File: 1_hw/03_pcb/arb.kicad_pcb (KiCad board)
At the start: 4 copper layers, 100 x 100 mm, 268 parts, among them J1 TYPE-C-31-M-12, J2 SMA, J3 SMA, J4 BNC, J5 PH-00244, SW1 TS-1187A-B-A-B, SW2 SS-12D02-VG4, SW3 SS-12D02-VG4, U1 TLV70333DBV, U10 LMK1C1103PWR, U11 STM32F446ZETx, U12 ICE40UP5K-SG48ITR, U13 93LC56BT-I_OT, U14 FT2232HL, U15 W25Q128JVSIQ, U16 W25Q128JVSIQ, U17 AD9850, U18 AD9744, U19 LM6171, U2 TLV76133DCY, U20 LM6171, U21 TMUX6104, U22 TPL0401B-10, U23 THS3491, U24 ADG1219BRJZ, U25 LM6171, U26 TMUX6104, U3 TLV70333DBV, U4 LM3880MF-1AA, U5 TLV70312DBV, U6 TLV70325DBV, U7 TPS65131RGE, U8 TPD2E001DRL, U9 ADG1219BRJZ, X1 ASE-10.000MHz, X2 ASE-100.000MHz, Y1 32.768k, Y2 12 MHz

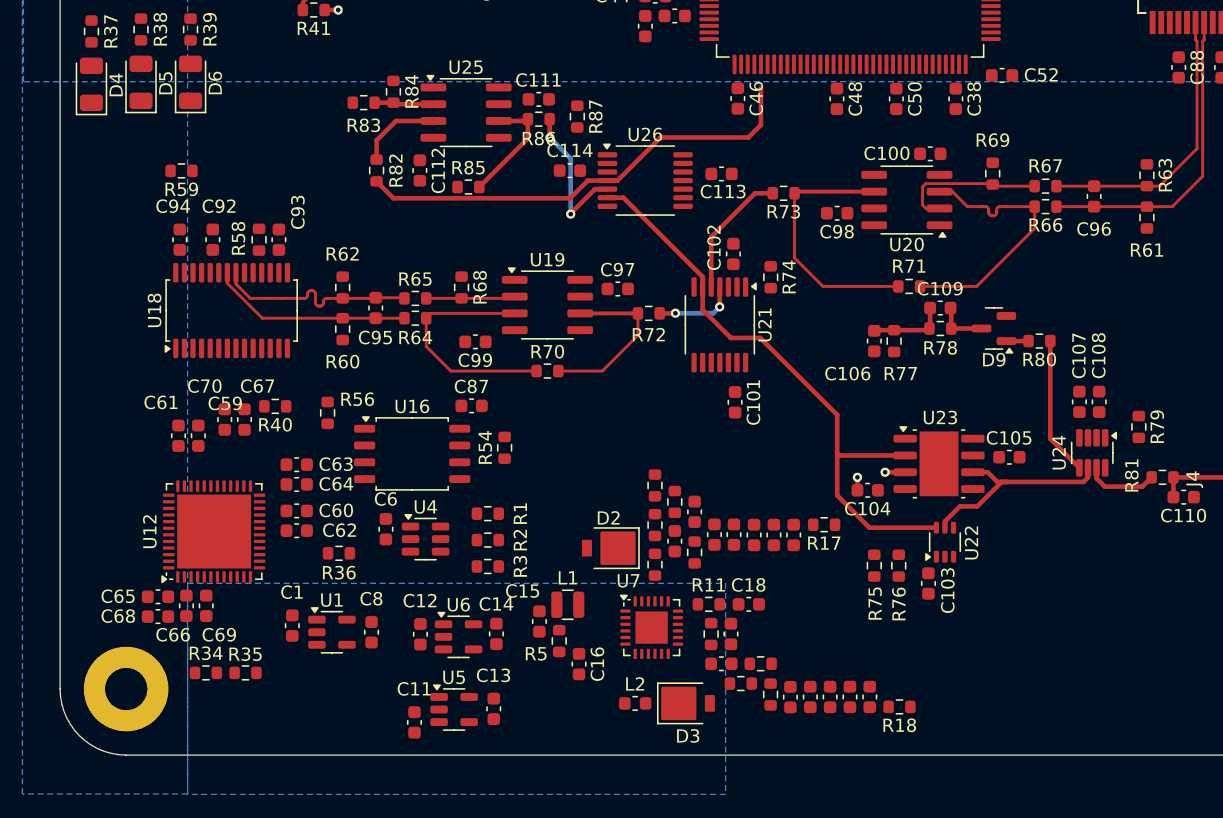
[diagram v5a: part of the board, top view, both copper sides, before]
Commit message: MINOR: Continuing layout. Laid Out FPGA Power.
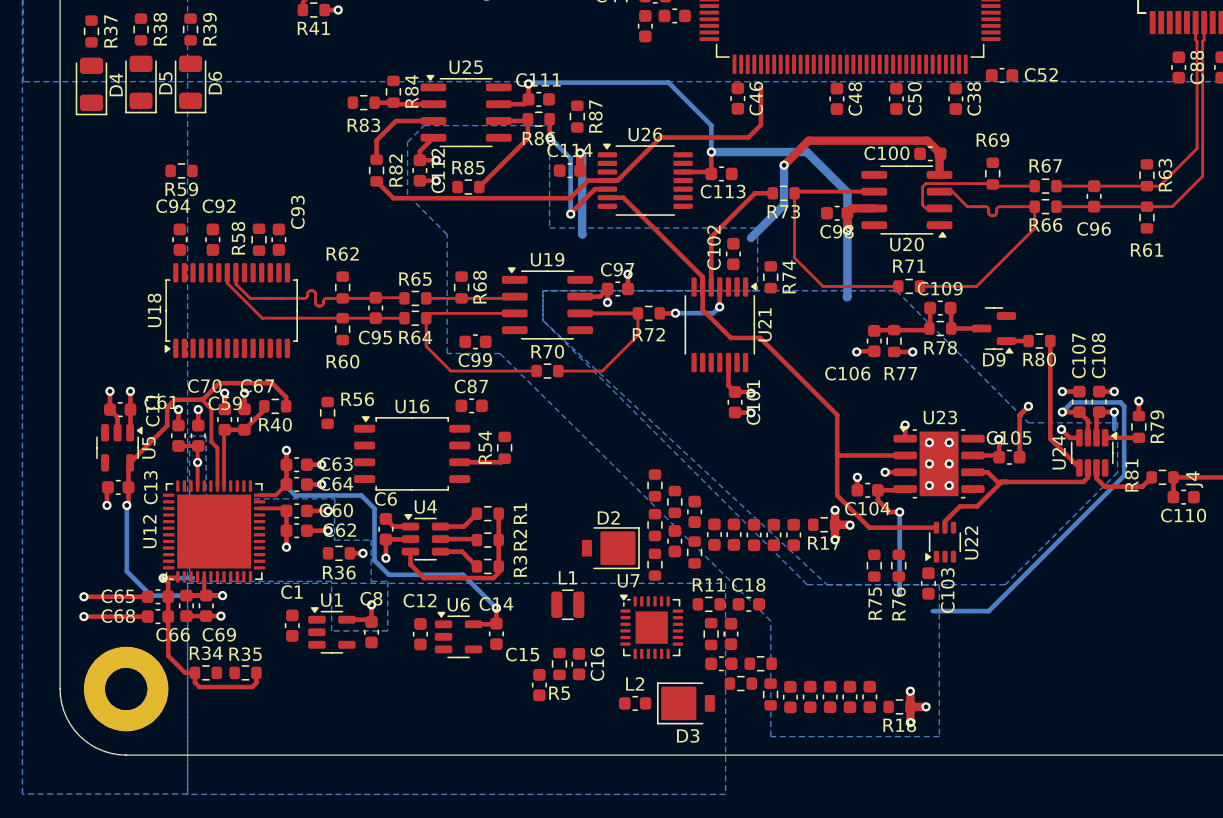
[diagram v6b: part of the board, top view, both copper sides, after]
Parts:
- moved C13 33.0 mm to (105.1, 122.7), turned to 180 degrees
- moved C11 32.5 mm to (105.2, 116.8), turned to 180 degrees
- moved U5 32.3 mm to (105.0, 119.7), turned to -90 degrees
- moved C15 4.81 mm to (137.0, 137.7)
- moved R5 1.74 mm to (138.5, 136.1), turned to 90 degrees
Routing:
- net N15P0V_A: track 0.00 -> 79.4 mm, vias 0 -> 8
- net 15P0V_A: track 0.00 -> 66.0 mm, vias 0 -> 10
- net GND: track 64.7 -> 113.0 mm, vias 41 -> 72
- net 1P2V_D: track 0.00 -> 43.9 mm, vias 0 -> 2
- net 2P5V_D: track 0.00 -> 32.6 mm, vias 0 -> 2
- net 3P3V_D_FPGA: track 0.00 -> 32.1 mm, vias 0 -> 5
- net 3P3V_D: track 37.2 -> 50.0 mm
- net Net-(U12D-VCCPLL): track 0.00 -> 8.18 mm
- net 5P0V: track 16.4 -> 21.7 mm, vias 8 -> 9
- net SPI_SCLK_MCU_FPGA_3P3: track 0.00 -> 3.51 mm
- net GPIO_2P5-EN_SEQ_REG_3P3: track 0.00 -> 3.22 mm
- net GPIO_1P2-EN_SEQ_REG_3P3: track 0.00 -> 3.15 mm
- net GPIO_3P3-EN_SEQ_REG_3P3: track 0.00 -> 2.78 mm
- net GPIO_EN_MCU_AMUX2_3P3: track 0.00 -> 2.55 mm
- added copper zone on B.Cu, net 15P0V_A
- added copper zone on B.Cu, net 3P3V_D_FPGA
- added copper zone on B.Cu, net N15P0V_A

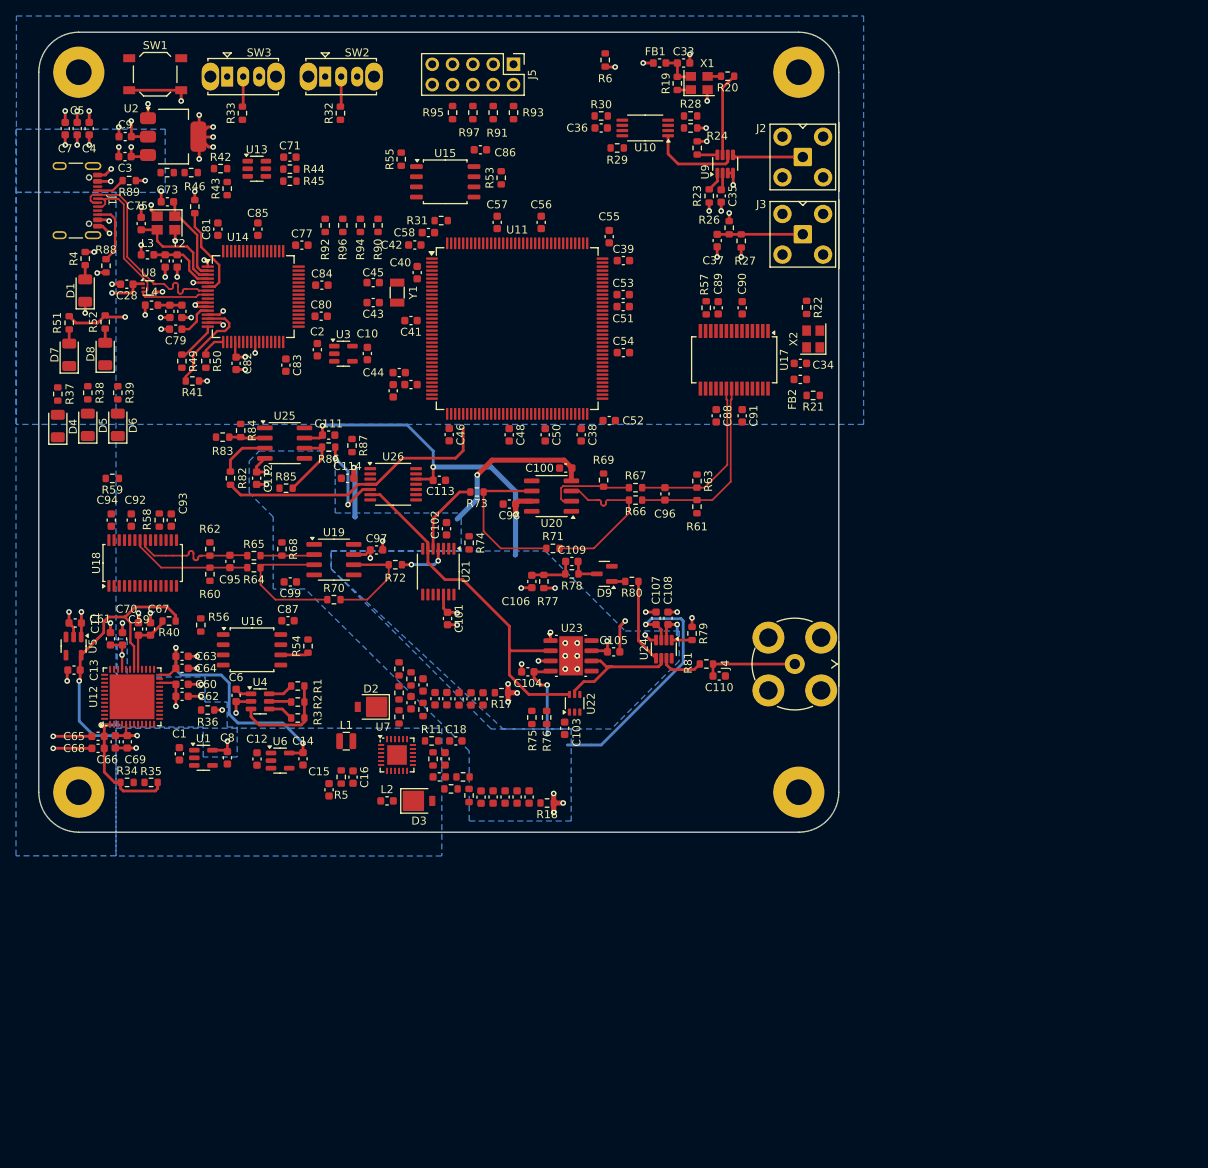
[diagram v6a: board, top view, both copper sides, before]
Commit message: MINOR: Layout. 3.3V Analog Power, FTDI IC. Clocks.
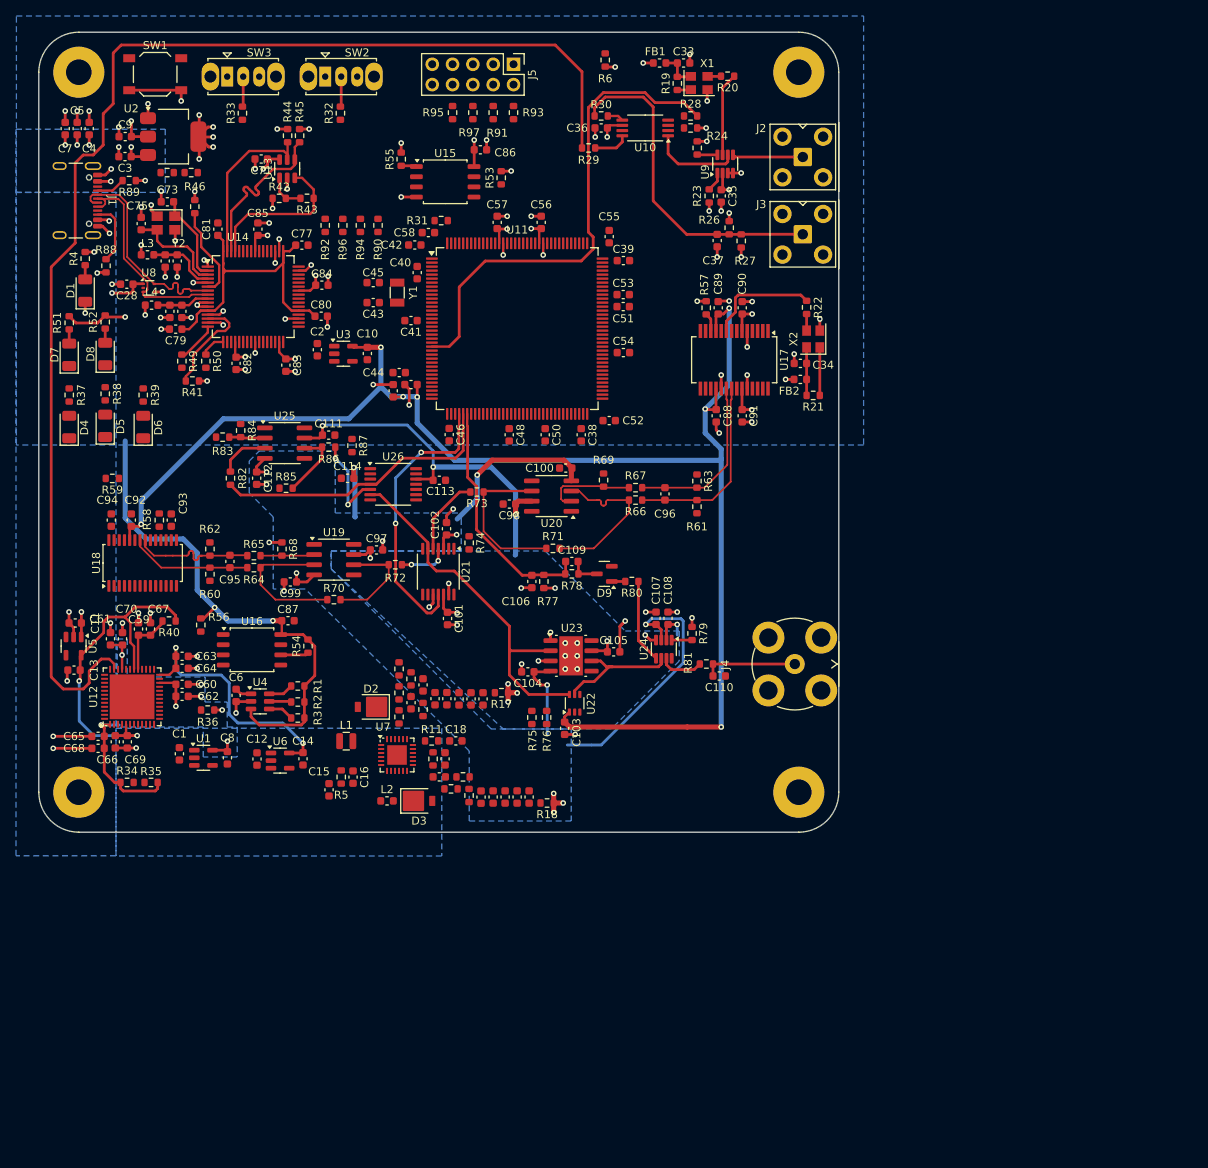
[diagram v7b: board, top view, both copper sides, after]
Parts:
- moved R43 10.1 mm to (134.2, 63.7), turned to 180 degrees
- moved R42 8.21 mm to (130.8, 63.7)
- moved R45 5.82 mm to (133.3, 55.9), turned to -90 degrees
- moved R44 4.20 mm to (131.8, 55.9), turned to -90 degrees
- moved U13 3.80 mm to (131.8, 60.0), turned to 90 degrees
- moved C71 3.59 mm to (128.5, 58.8), turned to 180 degrees
- moved R29 3.57 mm to (169.4, 57.4)
- moved D6 3.19 mm to (113.8, 92.3)
- moved R39 3.19 mm to (113.8, 88.3)
- moved D5 2.18 mm to (109.0, 92.2)
- moved R38 2.18 mm to (109.0, 88.2)
- moved D4 1.43 mm to (104.5, 92.3)
- moved R37 1.43 mm to (104.5, 88.3)
- turned FB2 to 0 degrees
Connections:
- U11 pad 34: ANALOG_CAL-ADC_AMUX2_MCU -> unconnected-(U11-PA0-Pad34)
- U11 pad 42: unconnected-(U11-PA6-Pad42) -> ANALOG_CAL-ADC_AMUX2_MCU
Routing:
- net 3P3V_A: track 0.00 -> 185.3 mm, vias 0 -> 7
- net CLK_10MHZ_DIST_FPGA_3P3: track 0.00 -> 163.7 mm
- net 3P3V_D: track 50.0 -> 145.2 mm, vias 15 -> 35
- net CLK_10MHZ_DIST_MCU_3P3: track 0.00 -> 62.4 mm
- net GND: track 113.0 -> 163.9 mm, vias 72 -> 106
- net ANALOG_DAC1_MCU_AMUX1: track 0.00 -> 35.5 mm, vias 0 -> 2
- net 1P8V_D: track 4.70 -> 38.7 mm
- net CLK_10MHZ_DIST_EXT_3P3: track 10.7 -> 41.6 mm
- net ANALOG_CAL-ADC_AMUX2_MCU: track 5.82 -> 30.0 mm
- net Net-(U13-CS): track 0.00 -> 21.4 mm
- net Net-(U13-CLK): track 0.00 -> 21.4 mm
- net Net-(U13-DI): track 0.00 -> 19.3 mm
- net CLK_100MHZ_DDS_3P3: track 0.00 -> 14.0 mm
- net N15P0V_A: track 79.4 -> 86.3 mm, vias 8 -> 10
- net Net-(X2-Vdd): track 0.00 -> 6.00 mm
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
